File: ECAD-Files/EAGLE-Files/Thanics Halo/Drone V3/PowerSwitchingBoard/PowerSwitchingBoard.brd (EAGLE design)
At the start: 80 x 88 mm, 252 parts, among them J1 ESC_CONTACTS, J3 62674-301121ALF, J4 B3B-ZR-SM4, J5 B3B-ZR-SM4, J6 B3B-ZR-SM4, Q1 500mA/300V, Q19 500mA/300V, Q2 500mA/300V, Q20 IRLR8726, Q21 IRLR8726, Q22 500mA/300V, Q23 IRLR8726, Q24 IRLR8726, Q25 500mA/300V, Q26 IRLR8726, Q27 IRLR8726, Q28 500mA/300V, Q29 IRLR8726, Q3 500mA/300V, Q30 IRLR8726, Q31 500mA/300V, Q32 IRLR8726, Q33 IRLR8726, Q34 500mA/300V, Q35 IRLR8726, Q36 IRLR8726, Q37 500mA/300V, Q38 IRLR8726, Q39 IRLR8726, Q4 IRLR8726, Q40 500mA/300V, Q41 IRLR8726, Q42 IRLR8726, Q43 500mA/300V, Q44 IRLR8726, Q45 IRLR8726, Q5 IRLR8726, Q6 IRLR8726, Q7 IRLR8726, Q8 IRLR8726, Q9 IRLR8726, U1 TPS65261RHBR, U10 MEGA8-AI, U11 MEGA8-AI, U2 74HC4052PW, U3 74HC4052PW, U4 DRV8313, U5 DRV8313, U6 DRV8313, U7 STM32F103RCT6LQFP-64-M, U8 MEGA8-AI, U9 MEGA8-AI, X1 16MHz, X3 16MHz, X4 16MHz, X5 16MHz, X6 8MHz

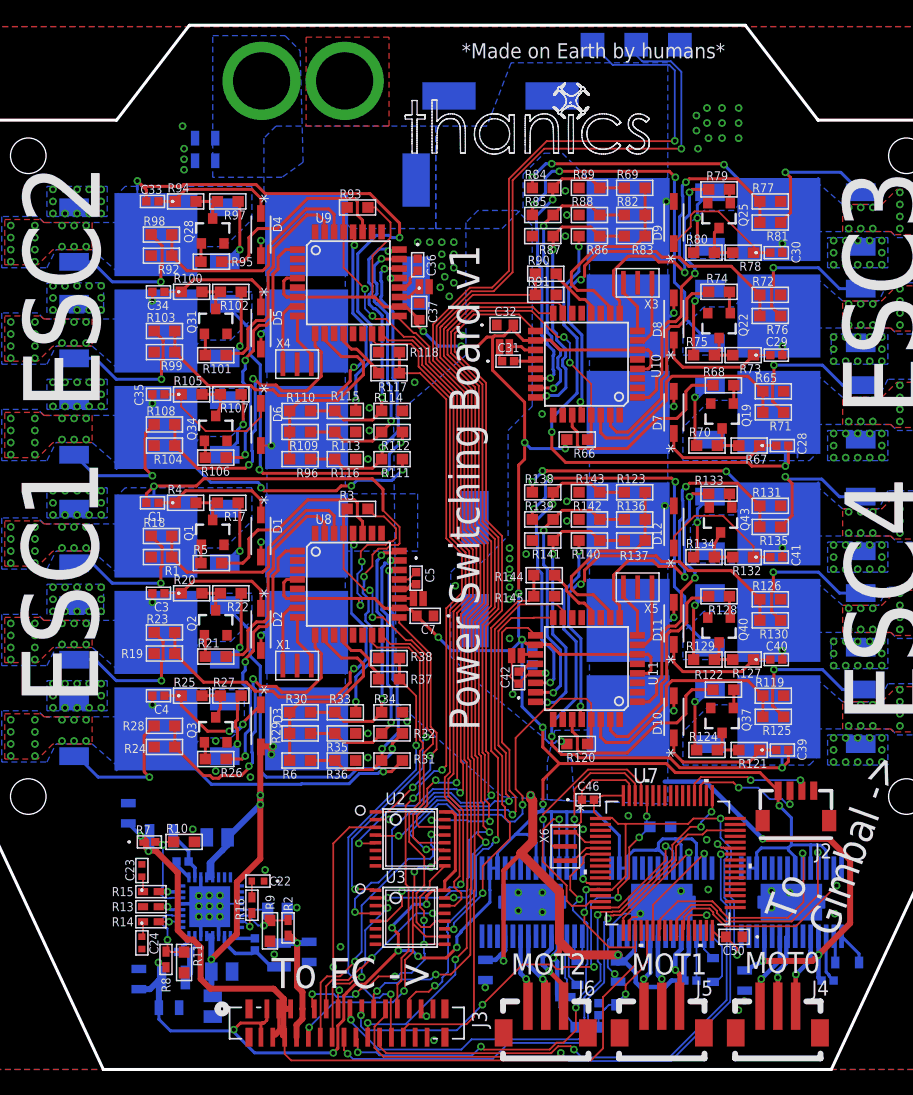
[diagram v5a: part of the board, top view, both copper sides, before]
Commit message: Created TOF Altimeter Board v1, and made power board 4 layers
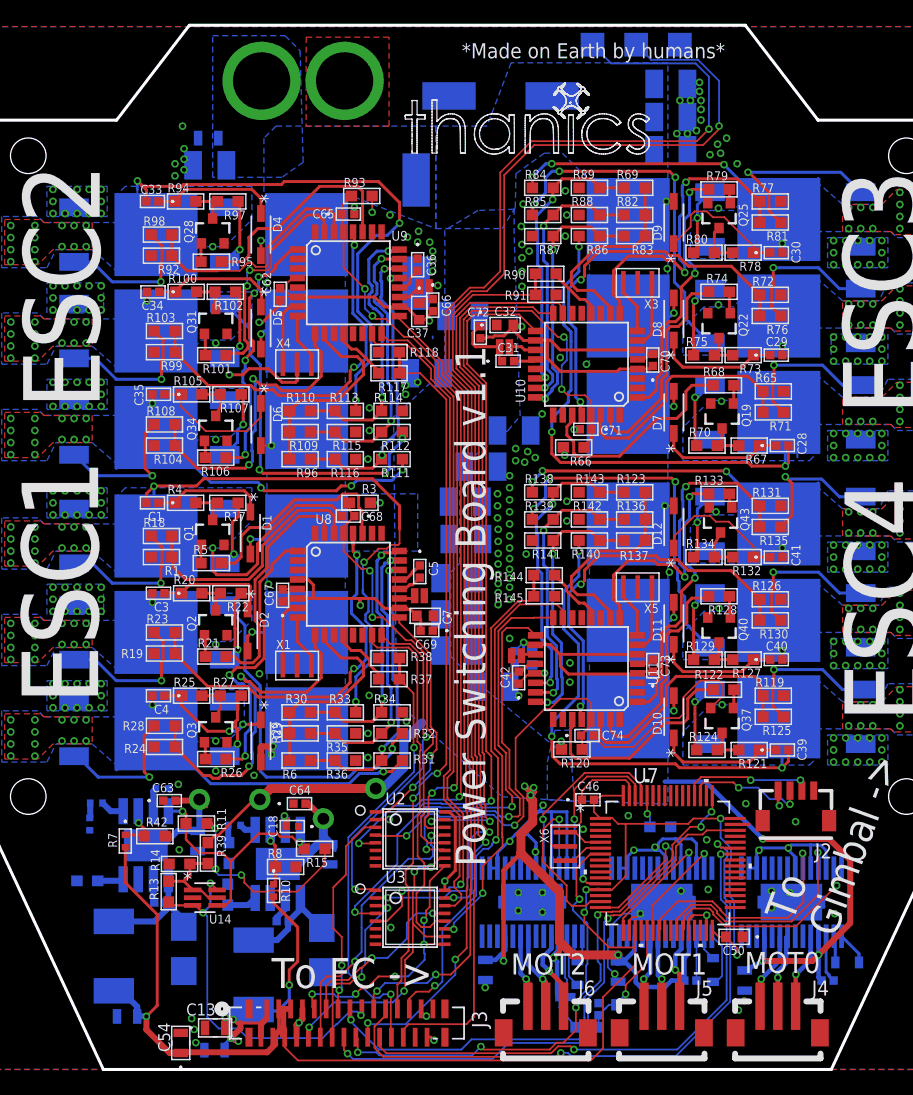
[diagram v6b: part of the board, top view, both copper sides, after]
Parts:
- removed L3: 4.7uH, 4.7uH-inductor:1008
- removed R16: 20k, 20k-resistor:RC0402N-M
- removed U1: TPS65261RHBR, tps65261:RHB32_3P45X3P45
- added C52, C54, C55: 22uF, 22uF X5R Ceramic Capacitor:G-21
- added C53, C62, C63, C64, C65, C66, C67, C68, C69, C70, C71, C72, C73, C74, C75: 0.1uF, 0.1uF-capacitor-0402:0402-M
- added C56: 2.2nF, thanics_robotics:0402_CAPACITOR
- added C57, C58, C59, C60, C61: 22uF, thanics_robotics:1210_CAPACITOR
- added D13, D14: SSB44-E3/52T, ssb44-schottky:DIODE_DO214AA_MBRS-M
- added F1, F2: 0ZRB0400FF1A, ptc-fuse:0ZRB0400FF1A
- added R39: 2.2k, 2.2k-resistor:RC0603N-M
- added R42: 10k (1%), 10k-resistor(0603):RC0603N-M
- added R43: 100k, 100k-resistor:RC0603N-M
- added R44: 47k, 47k-resistor:RC0603N-M
- added U12, U13: AOZ1284, thanics_robotics:EPAD_SO-8
- added U14: SN74LVC1G373DCKRDCK6-M, d-latch:DCK6-M
- C13: value 10uF -> 22uF; device thanics_robotics:0805_CAPACITOR -> 22uF X5R Ceramic Capacitor:G-21
- C15, C16: value 0.1uF -> 22uF; device 0.1uF-capacitor-0402:0402-M -> 22uF X5R Ceramic Capacitor:G-21
- C17: value 1uF -> 2.2nF; device 1uF X7R Ceramic Capacitor:YAG_CC0805 -> thanics_robotics:0402_CAPACITOR
- C18, C2: value 10uF -> 1nF; device thanics_robotics:0805_CAPACITOR -> 1000pF-capacitor:G-155-M
- C19, C20, C21, C25, C8: device 22uF X5R Ceramic Capacitor:G-21 -> thanics_robotics:1210_CAPACITOR
- C22, C23, C24: value 2.2nF -> 22uF; device thanics_robotics:0402_CAPACITOR -> thanics_robotics:1210_CAPACITOR
- C48: value 470uF -> 22uF; device 470uF-capacitor:PCAP_10X10-ELECT-M -> thanics_robotics:1210_CAPACITOR
- L1, L2: value 4.7uH -> 10uH; device 4.7uH-inductor:1008 -> thanics_robotics:PA431.XXX
- R10: value 10k -> 52.3k (1%); device 10k-resistor(0603):RC0603N-M -> thanics_robotics:0402_CAPACITOR
- R11: value 10k -> 100k; device 10k-resistor(0603):RC0603N-M -> 100k-resistor:RC0603N-M
- R13: value 73.2k -> 100k; device 45.3k-resistor:RC0402N-M -> 100k-resistor:RC0603N-M
- R14: value 20k -> 1k; device 20k-resistor:RC0402N-M -> 1k-resistor:RC0603N-M
- R15: value 20k -> 100k; device 20k-resistor:RC0402N-M -> 100k-resistor:RC0603N-M
- R2: value 10k -> 31.6k (1%); device 10k-resistor(0603):RC0603N-M -> thanics_robotics:0402_CAPACITOR
- R7: value 45.3k -> 31.6k (1%); device 73.2k-resistor:STA_RMCF0402-M -> thanics_robotics:0402_CAPACITOR
- R8: value 73.2k -> 10k (1%); device 45.3k-resistor:RC0402N-M -> 10k-resistor(0603):RC0603N-M
- R9: value 20k -> 47k; device 20k-resistor:RC0402N-M -> 47k-resistor:RC0603N-M
- moved C24 59.4 mm to (39.6, 63.5), flipped to the bottom, turned to 180 degrees
- moved C25 49.8 mm to (36.6, 58.7), turned to 180 degrees
- moved C23 48.6 mm to (43.9, 53.8), flipped to the bottom, turned to 0 degrees
- moved C20 43.1 mm to (39.1, 41.4), turned to 0 degrees
- moved C21 41.1 mm to (39.1, 38.4)
- moved C22 39.7 mm to (41.1, 50.8), flipped to the bottom, turned to 0 degrees
- moved C8 38.7 mm to (39.9, 44.7)
- moved C19 38.7 mm to (39.8, 47.9), turned to 0 degrees
- moved R2 17.7 mm to (8.18, 20.7), flipped to the bottom, turned to 90 degrees
- moved C2 16.2 mm to (14.3, 23.7)
- moved C15 16.1 mm to (18.7, 1.63)
- moved C16 14.8 mm to (28.4, 18.1), turned to 90 degrees
- moved R15 14.3 mm to (27.1, 18.6), turned to 180 degrees
- moved L2 14.1 mm to (22.0, 7.98), turned to 270 degrees
- moved L1 13.9 mm to (10.2, 9.55)
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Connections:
- removed net +1V8: C25.2, J3.7, J3.8, L1.P$1, R9.1
- removed net N$16: C15.2, U1.25
- removed net N$20: C14.2, L1.P$2, U1.10
- removed net N$23: C17.2, U1.5
- removed net N$26: R16.1, U1.7
- removed net N$27: C22.2, R16.2
- removed net N$28: R15.2, U1.23
- removed net N$29: C23.1, R15.1
- new net EN: R11.2, R15.2, U12.8, U13.8, U14.4
- new net N$49: C53.1, U12.2
- new net N$50: C53.2, D13.1, L1.P$1, U12.1
- new net N$51: R42.1, R7.1, U12.6
- new net N$52: R43.1, U12.4
- new net PWR_EN: J3.18, R13.2, U14.3, U14.6
- new net V2FUSED: C16.2, C64.2, F2.2, U13.EP
- new net VFUSED: C55.2, C63.2, F1.2, U12.EP
- new net V_LATCH: R11.1, R13.1, R14.1, R15.1, R39.2, U14.1, U14.5
- net +3V3: now also C52.2, C54.1, L1.P$2, R7.2; no longer C19.2, L2.P$2, R7.1
- net +5V: now also C13.2, C15.1, C62.1, C66.2, C67.1, C69.2, C70.1, C72.2, C73.1, C75.2, L2.P$2, R10.2; no longer C20.2, C21.2, L3.P$2, R8.2
- net BOOT0: no longer J3.18
- net GND: now also C15.2, C16.1, C23.1, C24.1, C52.1, C54.2, C55.1, C57.2, C58.2, C59.2, C60.2, C61.2, C62.2, C63.1, C64.1, C65.2, C66.1, C67.2, C68.2, C69.1, C70.2, C71.2, C72.1, C73.2, C74.2, C75.1, C8.1, D13.2, D14.2, J3.7, J3.8, R14.2, R2.1, R42.2, R43.2, R44.2, R8.2, R9.2, U12.3, U13.3, U14.2; no longer C17.1, C23.2, C24.2, C8.2, R10.2, R11.2, R13.1, R2.2, U1.11, U1.14, U1.21, U1.27, U1.33, U1.4
- net N$11: now also C2.2, U12.7; no longer C14.1, U1.9
- net N$12: now also C14.1, U13.2; no longer R14.2, U1.18
- net N$13: now also C14.2, D14.1, L2.P$1, U13.1; no longer R2.1, R9.2, U1.6
- net N$14: now also R10.1, R8.1, U13.6; no longer R13.2, U1.20
- net N$15: now also R44.1, U13.4; no longer C15.1, L2.P$1, U1.26
- net N$17: now also C17.2, U13.5; no longer R10.1, R7.2, U1.22
- net N$18: now also C17.1, R9.1; no longer C24.1, R14.1
- net N$19: now also C18.2, U13.7; no longer C16.1, L3.P$1, U1.15
- net N$2: now also C56.2, U12.5; no longer C16.2, U1.16
- net N$3: now also C56.1, R2.2; no longer R11.1, R8.1, U1.19
- net RST1: now also C68.1
- net RST2: now also C65.1
- net RST3: now also C71.1
- net RST4: now also C74.1
- net VDD: now also C19.2, C20.2, C21.2, C22.2, C23.2, C24.2, C25.2, C57.1, C58.1, C59.1, C60.1, C61.1, C8.2, F1.1, F2.1, R39.1; no longer C13.2, C18.2, C2.2, C8.1, U1.12, U1.13, U1.28, U1.29
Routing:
- net +5V: track 307.2 -> 182.8 mm, vias 21 -> 23
- net GND: track 47.9 -> 93.3 mm, vias 237 -> 287
- net BOOT0: track 41.6 -> 2.73 mm, vias 6 -> 1
- net PWR_EN: track 0.00 -> 31.1 mm, vias 0 -> 3
- net V_LATCH: track 0.00 -> 26.6 mm, vias 0 -> 3
- net EN: track 0.00 -> 21.9 mm, vias 0 -> 2
- net +1V8: track 11.9 -> 0.00 mm, vias 1 -> 0
- net VFUSED: track 0.00 -> 10.6 mm
- net V2FUSED: track 0.00 -> 10.2 mm
- net N$50: track 0.00 -> 10.1 mm
- net +3V3: track 123.4 -> 131.1 mm, vias 6 -> 5
- net VDD: track 196.0 -> 188.8 mm, vias 23 -> 22
- net N$17: track 7.78 -> 1.39 mm, vias 1 -> 0
- net N$20: track 6.20 -> 0.00 mm
- net N$3: track 6.20 -> 1.27 mm, vias 1 -> 0
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- added copper zone on layer 2, net +5V
- added copper zone on layer 15, net GND
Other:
- board text added: "Power Switching Board v1.1"
- board text added: "To Batt->"
- board text removed: "Power Switching Board v1"
- board text removed: "To Batt ->"

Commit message: finished power board v1.2
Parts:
- removed R42: 10k (1%), 10k-resistor(0603):RC0603N-M
- removed R43: 100k, 100k-resistor:RC0603N-M
- removed R44: 47k, 47k-resistor:RC0603N-M
- removed U13: AOZ1284, thanics_robotics:EPAD_SO-8
- added R16: 10.2k, thanics-resistor:R0402
- added U1: TPS54331DRD8-M, tps54331:D8-M
- C13, C15, C16: device 22uF X5R Ceramic Capacitor:G-21 -> thanics_robotics:1210_CAPACITOR
- C14: value 0.1uF -> 10nF; device 0.1uF-capacitor-0402:0402-M -> thanics_robotics:0603_CAPACITOR
- C17: value 2.2nF -> 22uF; device thanics_robotics:0402_CAPACITOR -> thanics_robotics:1210_CAPACITOR
- C18: device 1000pF-capacitor:G-155-M -> thanics-capacitor:C0402
- C2: value 1nF -> 22uF; device 1000pF-capacitor:G-155-M -> thanics_robotics:1210_CAPACITOR
- C26: value 10uF -> 0.1uF; device 10uF X5R Ceramic Capacitor:G-21 -> 0.1uF-capacitor-0402:0402-M
- C44: value 10uF -> 43pF; device 10uF X5R Ceramic Capacitor:G-21 -> thanics-capacitor:C0603
- C47: value 10uF -> 22uF; device 10uF X5R Ceramic Capacitor:G-21 -> thanics-capacitor:C0805
- C52: value 22uF -> 10nF; device 22uF X5R Ceramic Capacitor:G-21 -> thanics_robotics:0603_CAPACITOR
- C53: value 0.1uF -> 2.2nF; device 0.1uF-capacitor-0402:0402-M -> thanics_robotics:0402_CAPACITOR
- C54: value 22uF -> 0.1uF; device 22uF X5R Ceramic Capacitor:G-21 -> 0.1uF-capacitor-0402:0402-M
- C55: value 22uF -> 43pF; device 22uF X5R Ceramic Capacitor:G-21 -> thanics-capacitor:C0603
- C56: value 2.2nF -> 22uF; device thanics_robotics:0402_CAPACITOR -> thanics-capacitor:C0805
- C63, C64: value 0.1uF -> 22uF; device 0.1uF-capacitor-0402:0402-M -> thanics-capacitor:C0805
- R10: value 52.3k (1%) -> 10.2k; device thanics_robotics:0402_CAPACITOR -> thanics-resistor:R0402
- R2: value 31.6k (1%) -> 3.24k; device thanics_robotics:0402_CAPACITOR -> thanics-resistor:R0603
- R7: value 31.6k (1%) -> 28.7k; device thanics_robotics:0402_CAPACITOR -> thanics-resistor:R0402
- R8: value 10k (1%) -> 1.96k; device 10k-resistor(0603):RC0603N-M -> thanics-resistor:R0603
- R9: value 47k -> 39.2k; device 47k-resistor:RC0603N-M -> thanics-resistor:R0402
- U12: value AOZ1284 -> TPS54331DRD8-M; device thanics_robotics:EPAD_SO-8 -> tps54331:D8-M
- moved C13 57.1 mm to (74.4, 16.4), turned to 180 degrees
- moved C26 43.6 mm to (20.6, 15.7), turned to 270 degrees
- moved C15 35.0 mm to (53.1, 7.87), turned to 90 degrees
- moved C44 25.9 mm to (27.9, 15.7), flipped to the top, turned to 0 degrees
- moved C47 25.4 mm to (16.4, 4.95), turned to 0 degrees
- moved C64 21.3 mm to (17.5, 2.79), flipped to the bottom
- moved C63 19.3 mm to (12.2, 3.56), flipped to the bottom, turned to 270 degrees
- moved C56 18.9 mm to (9.91, 3.56), turned to 270 degrees
- moved C16 17.6 mm to (42.2, 7.11)
- moved C54 15.9 mm to (7.24, 15.6), flipped to the bottom, turned to 270 degrees
- moved C52 15.6 mm to (14.4, 19.8), turned to 90 degrees
- moved R2 12.4 mm to (15.9, 10.9), flipped to the top, turned to 180 degrees
- moved C55 12.4 mm to (6.10, 13.8), flipped to the top, turned to 180 degrees
- moved C17 9.06 mm to (28.7, 17.0), turned to 270 degrees
- moved R9 8.58 mm to (27.6, 14.4), flipped to the top, turned to 180 degrees
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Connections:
- removed net N$49: C53.1, U12.2
- removed net N$50: C53.2, D13.1, L1.P$1, U12.1
- removed net N$51: R42.1, R7.1, U12.6
- removed net N$52: R43.1, U12.4
- new net N$16: C26.1, U1.1
- new net N$20: R16.1, R2.2, U12.5
- net +3V3: now also C56.1, C63.1, R16.2; no longer C52.2, C54.1, R7.2
- net +5V: now also C47.1, C64.1; no longer C13.2, C15.1
- net EN: now also R15.1, U1.3, U12.3; no longer R15.2, U12.8, U13.8
- net GND: now also C14.1, C15.1, C17.2, C18.2, C2.2, C44.2, C47.2, C53.1, C55.2, C56.2, C63.2, C64.2, R8.1, U1.7, U1.EP, U12.7, U12.EP; no longer C15.2, C18.1, C2.1, C26.1, C44.1, C47.1, C54.2, C55.1, C63.1, C64.1, R42.2, R43.2, R44.2, R8.2, R9.2, U12.3, U13.3
- net N$11: now also C52.2, U12.4; no longer C2.2, U12.7
- net N$12: now also C54.1, U12.1; no longer C14.1, U13.2
- net N$13: now also C44.1, R9.2, U1.6; no longer C14.2, D14.1, L2.P$1, U13.1
- net N$14: now also C18.1, R9.1; no longer R10.1, R8.1, U13.6
- net N$15: now also C14.2, U1.4; no longer R44.1, U13.4
- net N$17: now also C26.2, D14.1, L2.P$1, U1.8; no longer C17.2, U13.5
- net N$18: now also C54.2, D13.1, L1.P$1, U12.8; no longer C17.1, R9.1
- net N$19: now also R10.1, R8.2, U1.5; no longer C18.2, U13.7
- net N$2: now also C55.1, R7.2, U12.6; no longer C56.2, U12.5
- net N$3: now also C53.2, R7.1; no longer C56.1, R2.2
- net V2FUSED: now also C17.1, U1.2; no longer C16.2, C64.2, U13.EP
- net VDD: now also C13.2, C15.2, C16.2; no longer C26.2, C44.2, C47.2
- net VFUSED: now also C2.1, U12.2; no longer C55.2, C63.2, U12.EP
- net V_LATCH: now also R15.2; no longer R15.1
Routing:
- net V_LATCH: track 26.6 -> 13.6 mm, vias 3 -> 2
- net N$17: track 1.39 -> 11.7 mm
- net N$50: track 10.1 -> 0.00 mm
- net N$18: track 1.49 -> 11.5 mm
- net +3V3: track 131.1 -> 122.9 mm, vias 5 -> 8
- net N$20: track 0.00 -> 7.59 mm, vias 0 -> 1
- net PWR_EN: track 31.1 -> 37.8 mm, vias 3 -> 4
- net N$2: track 2.02 -> 6.52 mm, vias 0 -> 1
- net N$51: track 3.98 -> 0.00 mm, vias 1 -> 0
- net N$16: track 0.00 -> 3.94 mm
- net EN: track 21.9 -> 25.6 mm
- net N$14: track 4.82 -> 1.16 mm, vias 1 -> 0
- net N$13: track 8.88 -> 5.63 mm, vias 0 -> 1
- net GND: track 93.3 -> 90.2 mm, vias 287 -> 350
- net VDD: track 188.8 -> 191.7 mm
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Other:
- board text added: "Power Switching Board v1.2"
- board text removed: "Power Switching Board v1.1"

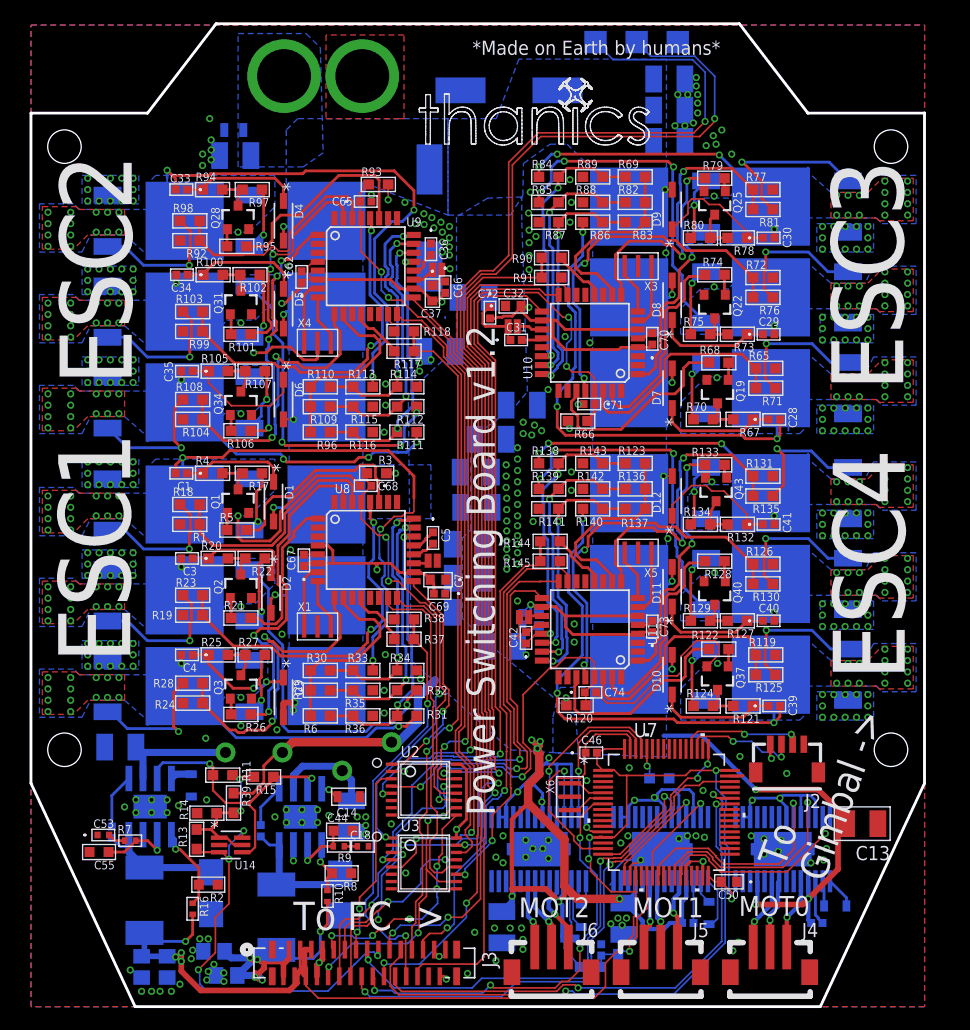
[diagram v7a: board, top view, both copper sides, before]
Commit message: About to remove touchscreen from controller board
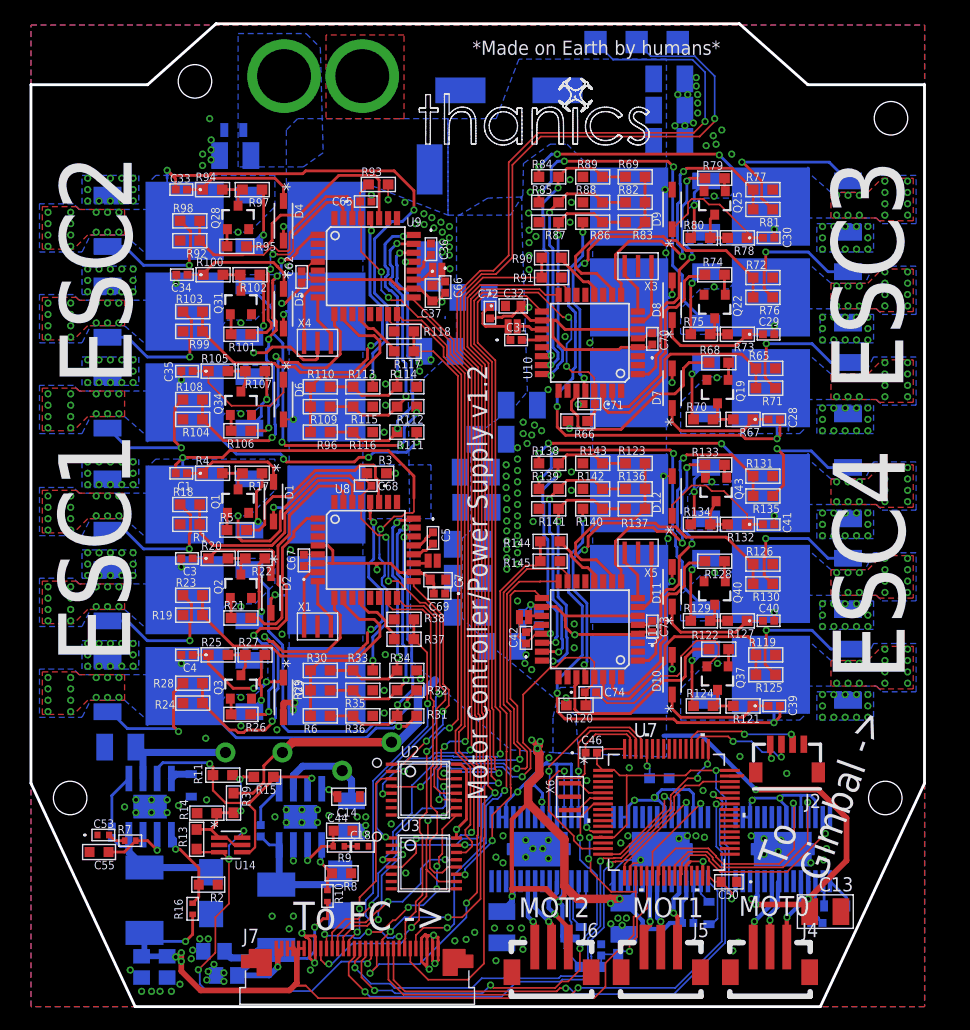
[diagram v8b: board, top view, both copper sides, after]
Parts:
- removed J3: 62674-301121ALF, 30pin_ffc_connector:CON30_1X30_DUT_58XF
- added J7: SFV30R-1STE1HLF, thanics-connector:SFV30R-1STE1HLF
- moved C13 8.54 mm to (71.1, 8.51)
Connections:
- net +3V3: now also J7.3, J7.4, J7.5, J7.6; no longer J3.3, J3.4, J3.5, J3.6
- net +5V: now also J7.1, J7.2; no longer J3.1, J3.2
- net BATT_SCL: now also J7.20; no longer J3.20
- net BATT_SDA: now also J7.19; no longer J3.19
- net GND: now also J7.27, J7.28, J7.29, J7.30, J7.7, J7.8; no longer J3.27, J3.28, J3.29, J3.30, J3.7, J3.8
- net MISO: now also J7.13; no longer J3.13
- net MOSI: now also J7.12; no longer J3.12
- net PWM: now also J7.23; no longer J3.23
- net PWM2: now also J7.24; no longer J3.24
- net PWM3: now also J7.25; no longer J3.25
- net PWM4: now also J7.26; no longer J3.26
- net PWR_EN: now also J7.18; no longer J3.18
- net RESET: now also J7.17; no longer J3.17
- net RST: now also J7.11; no longer J3.11
- net RX: now also J7.22; no longer J3.22
- net SCK: now also J7.14; no longer J3.14
- net SEL0: now also J7.9; no longer J3.9
- net SEL1: now also J7.10; no longer J3.10
- net SWCLK: now also J7.16; no longer J3.16
- net SWDIO: now also J7.15; no longer J3.15
- net TX: now also J7.21; no longer J3.21
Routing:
- net GND: track 90.2 -> 105.7 mm, vias 350 -> 360
- net +5V: track 181.3 -> 174.6 mm, vias 23 -> 21
- net +3V3: track 122.9 -> 117.9 mm
- net PWM: track 37.6 -> 34.3 mm
- net SWDIO: track 47.8 -> 51.0 mm
- net RESET: track 38.4 -> 41.5 mm
- net TX: track 46.1 -> 48.9 mm
- net BATT_SDA: track 116.3 -> 119.1 mm
- net PWM3: track 76.4 -> 79.0 mm
- net VDD: track 191.7 -> 194.2 mm, vias 22 -> 24
- net RST: track 23.9 -> 21.7 mm
- net MISO: track 14.9 -> 12.6 mm
- net SWCLK: track 48.3 -> 50.1 mm
- net RX: track 51.8 -> 50.9 mm
- net PWM4: track 43.0 -> 43.7 mm
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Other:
- outline, holes or cut-outs redrawn
- board text added: "Motor Controller/Power Supply v1.2"
- board text removed: "Power Switching Board v1.2"
